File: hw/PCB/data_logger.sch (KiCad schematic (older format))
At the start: 3 parts, among them J4 Micro_SD_Card_Det

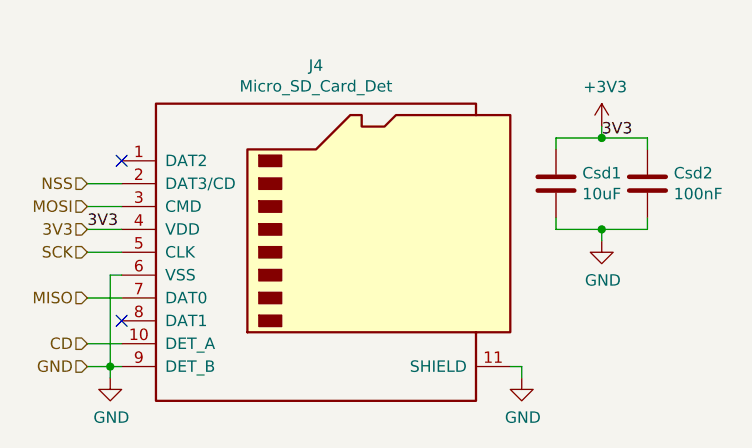
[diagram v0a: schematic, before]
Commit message: Added pullup resistor to the chip-select pin of the uSD card slot.
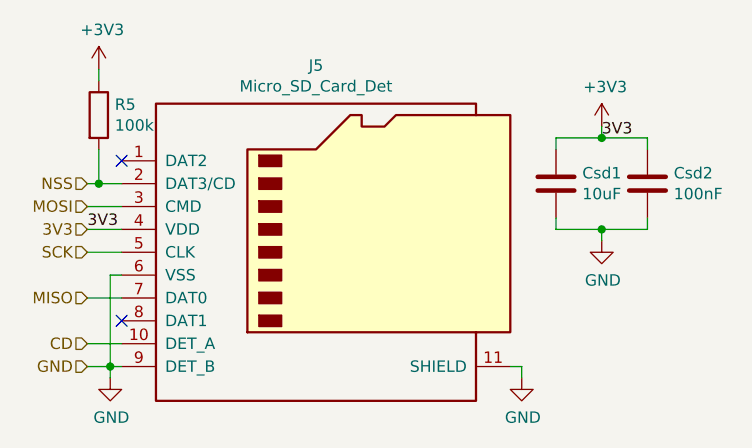
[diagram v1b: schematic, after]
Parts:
- added R5: 100k, Resistor_SMD:R_0603_1608Metric_Pad1.05x0.95mm_HandSolder, symbol Device:R
- Csd1, Csd2: footprint (none) -> Capacitor_SMD:C_0603_1608Metric_Pad1.05x0.95mm_HandSolder
- J5: renamed from J4; footprint (none) -> SD:microSD_socket
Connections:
- net +3V3: now also R5.1
- net NSS: now also R5.2
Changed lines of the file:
@@
 $EndDescr
 $Comp
-L Connector:Micro_SD_Card_Det J4
+L Connector:Micro_SD_Card_Det J5
 U 1 1 5D1D232F
 P 5600 3500
-F 0 "J4" H 5550 4317 50  0000 C CNN
+F 0 "J5" H 5550 4317 50  0000 C CNN
 F 1 "Micro_SD_Card_Det" H 5550 4226 50  0000 C CNN
-F 2 "" H 7650 4200 50  0001 C CNN
+F 2 "SD:microSD_socket" H 7650 4200 50  0001 C CNN
 F 3 "https://www.hirose.com/product/en/download_file/key_name/DM3/category/Catalog/doc_file_id/49662/?file_category_id=4&item_id=195&is_series=1" H 5600 3600 50  0001 C CNN
 	1    5600 3500
@@
 NoConn ~ 4700 3800
 Wire Wire Line
-	4550 3200 4700 3200
+	4550 3200 4600 3200
 Wire Wire Line
 	4700 3300 4550 3300
@@
 	6450 4000 6450 4050
 $Comp
-L power:GND #PWR?
+L power:GND #PWR0124
 U 1 1 5D1D4624
 P 6450 4050
-F 0 "#PWR?" H 6450 3800 50  0001 C CNN
+F 0 "#PWR0124" H 6450 3800 50  0001 C CNN
 F 1 "GND" H 6455 3877 50  0000 C CNN
 F 2 "" H 6450 4050 50  0001 C CNN
@@
 $EndComp
 $Comp
-L power:GND #PWR?
+L power:GND #PWR0125
 U 1 1 5D1D4B1C
 P 4650 4050
-F 0 "#PWR?" H 4650 3800 50  0001 C CNN
+F 0 "#PWR0125" H 4650 3800 50  0001 C CNN
 F 1 "GND" H 4655 3877 50  0000 C CNN
 F 2 "" H 4650 4050 50  0001 C CNN
@@
 	4650 4050 4650 4000
 $Comp
-L power:+3V3 #PWR?
+L power:+3V3 #PWR0126
 U 1 1 5D1F34BB
 P 6800 2950
-F 0 "#PWR?" H 6800 2800 50  0001 C CNN
+F 0 "#PWR0126" H 6800 2800 50  0001 C CNN
 F 1 "+3V3" H 6815 3123 50  0000 C CNN
 F 2 "" H 6800 2950 50  0001 C CNN
@@
 F 0 "Csd1" H 6715 3246 50  0000 L CNN
 F 1 "10uF" H 6715 3155 50  0000 L CNN
-F 2 "" H 6638 3050 50  0001 C CNN
+F 2 "Capacitor_SMD:C_0603_1608Metric_Pad1.05x0.95mm_HandSolder" H 6638 3050 50  0001 C CNN
 F 3 "~" H 6600 3200 50  0001 C CNN
 	1    6600 3200
@@
 F 0 "Csd2" H 7115 3246 50  0000 L CNN
 F 1 "100nF" H 7115 3155 50  0000 L CNN
-F 2 "" H 7038 3050 50  0001 C CNN
+F 2 "Capacitor_SMD:C_0603_1608Metric_Pad1.05x0.95mm_HandSolder" H 7038 3050 50  0001 C CNN
 F 3 "~" H 7000 3200 50  0001 C CNN
 	1    7000 3200
@@
 $EndComp
 $Comp
-L power:GND #PWR?
+L power:GND #PWR0127
 U 1 1 5D1F43D1
 P 6800 3450
-F 0 "#PWR?" H 6800 3200 50  0001 C CNN
+F 0 "#PWR0127" H 6800 3200 50  0001 C CNN
 F 1 "GND" H 6805 3277 50  0000 C CNN
 F 2 "" H 6800 3450 50  0001 C CNN
@@
 Text Label 6800 3000 0    50   ~ 0
 3V3
+$Comp
+L Device:R R5
+U 1 1 5D1D8E69
+P 4600 2900
+F 0 "R5" H 4670 2946 50  0000 L CNN
+F 1 "100k" H 4670 2855 50  0000 L CNN
+F 2 "Resistor_SMD:R_0603_1608Metric_Pad1.05x0.95mm_HandSolder" V 4530 2900 50  0001 C CNN
+F 3 "~" H 4600 2900 50  0001 C CNN
+	1    4600 2900
+	1    0    0    -1
+$EndComp
+Wire Wire Line
+	4600 3050 4600 3200
+Connection ~ 4600 3200
+Wire Wire Line
+	4600 3200 4700 3200
+Wire Wire Line
+	4600 2750 4600 2700
+$Comp
+L power:+3V3 #PWR0128
+U 1 1 5D1D96D0
+P 4600 2700
+F 0 "#PWR0128" H 4600 2550 50  0001 C CNN
+F 1 "+3V3" H 4615 2873 50  0000 C CNN
+F 2 "" H 4600 2700 50  0001 C CNN
+F 3 "" H 4600 2700 50  0001 C CNN
+	1    4600 2700
+	1    0    0    -1
+$EndComp
 $EndSCHEMATC
